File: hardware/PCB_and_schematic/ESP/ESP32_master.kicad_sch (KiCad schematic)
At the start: 0 parts

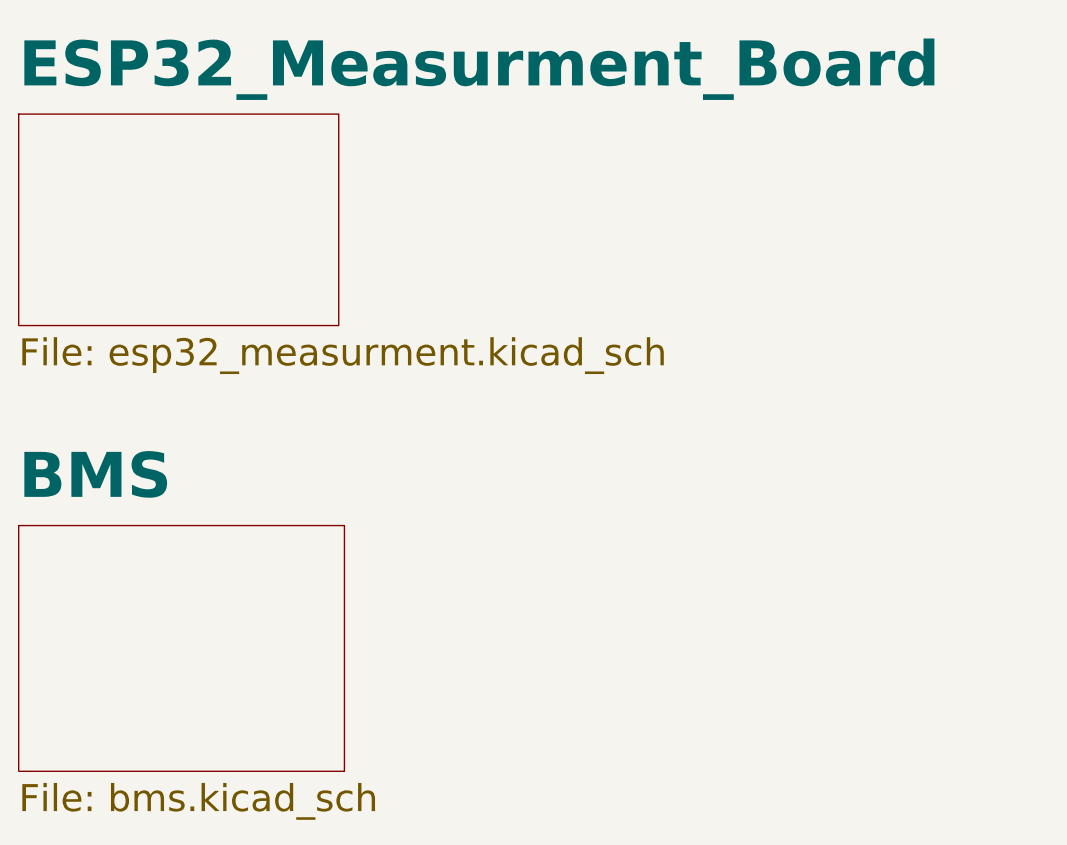
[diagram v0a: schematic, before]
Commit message: Add simulations and recheck schematics + cleanup
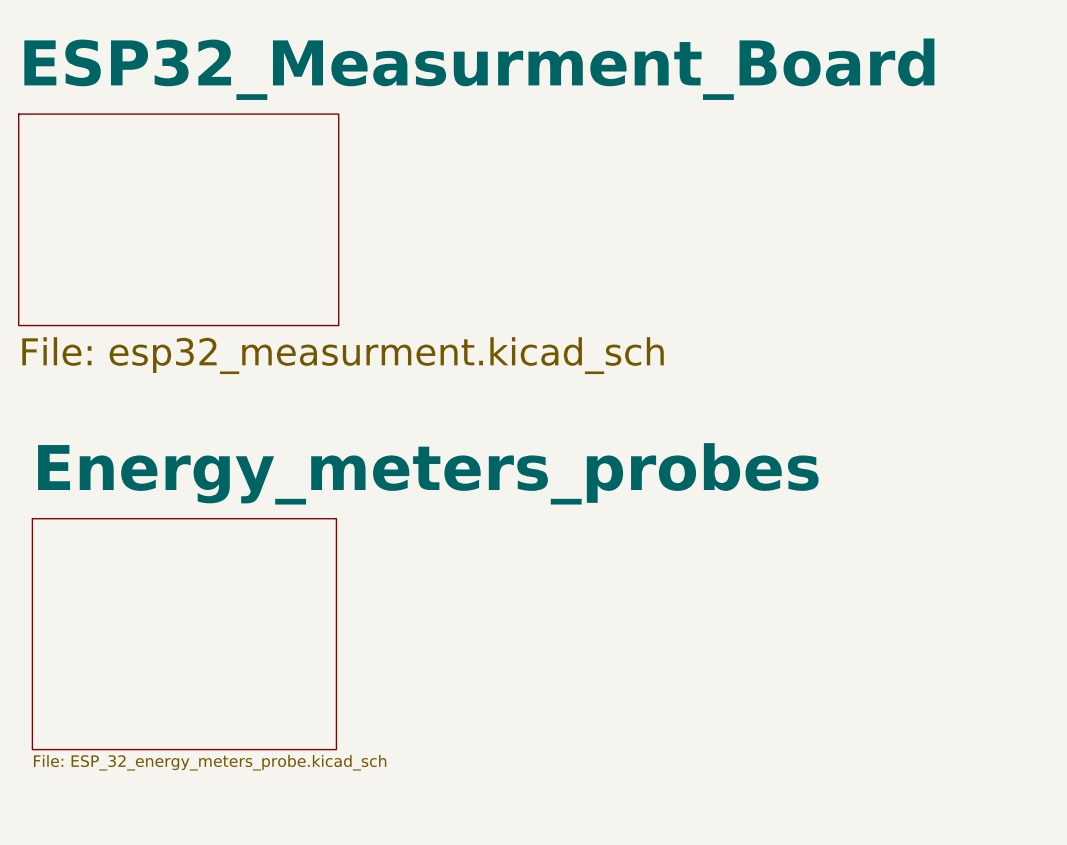
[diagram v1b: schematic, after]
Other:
- removed sheet BMS
- added sheet Energy_meters_probes (ESP_32_energy_meters_probe.kicad_sch)
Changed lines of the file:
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@@
 	(paper "A4" portrait)
 	(sheet
-		(at 24.13 80.01)
-		(size 36.195 27.305)
+		(at 25.654 79.248)
+		(size 33.782 25.654)
 		(fields_autoplaced yes)
 		(stroke
@@
 			(color 0 0 0 0.0000)
 		)
-		(property "Sheetname" "BMS"
-			(at 24.13 77.4334 0)
+		(property "Sheetname" "Energy_meters_probes"
+			(at 25.654 76.6714 0)
 			(effects
 				(font
@@
 			)
 		)
-		(property "Sheetfile" "bms.kicad_sch"
-			(at 24.13 108.5916 0)
+		(property "Sheetfile" "ESP_32_energy_meters_probe.kicad_sch"
+			(at 25.654 105.4866 0)
 			(effects
 				(font
-					(size 3 3)
+					(size 1.27 1.27)
 				)
 				(justify left top)
@@
 		)
 		(instances
-			(project "Balancer+ESP"
+			(project "ESP32_master"
 				(path "/555ba40f-9abb-4b99-82c6-07e888fda9fd"
 					(page "3")
@@
 		)
 		(instances
-			(project "Balancer+ESP"
+			(project "ESP32_master"
 				(path "/555ba40f-9abb-4b99-82c6-07e888fda9fd"
 					(page "2")

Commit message: Balancer routing
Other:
- removed sheet Energy_meters_probes
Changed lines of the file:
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@@
 	(paper "A4" portrait)
-	(sheet
-		(at 25.654 79.248)
-		(size 33.782 25.654)
-		(fields_autoplaced yes)
-		(stroke
-			(width 0.1524)
-			(type solid)
-		)
-		(fill
-			(color 0 0 0 0.0000)
-		)
-		(property "Sheetname" "Energy_meters_probes"
-			(at 25.654 76.6714 0)
-			(effects
-				(font
-					(size 5 5)
-					(bold yes)
-				)
-				(justify left bottom)
-			)
-		)
-		(property "Sheetfile" "ESP_32_energy_meters_probe.kicad_sch"
-			(at 25.654 105.4866 0)
-			(effects
-				(font
-					(size 1.27 1.27)
-				)
-				(justify left top)
-			)
-		)
-		(instances
-			(project "ESP32_master"
-				(path "/555ba40f-9abb-4b99-82c6-07e888fda9fd"
-					(page "3")
-				)
-			)
-		)
-	)
 	(sheet
 		(at 24.13 34.29)

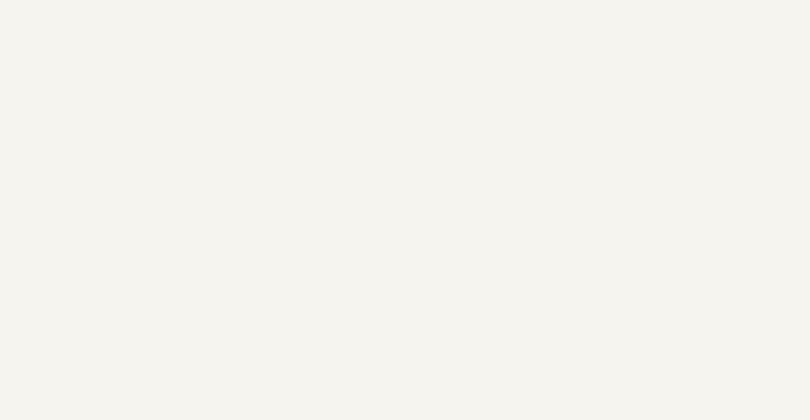
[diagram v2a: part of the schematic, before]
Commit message: Update of ESP32 PCB - parts positioning
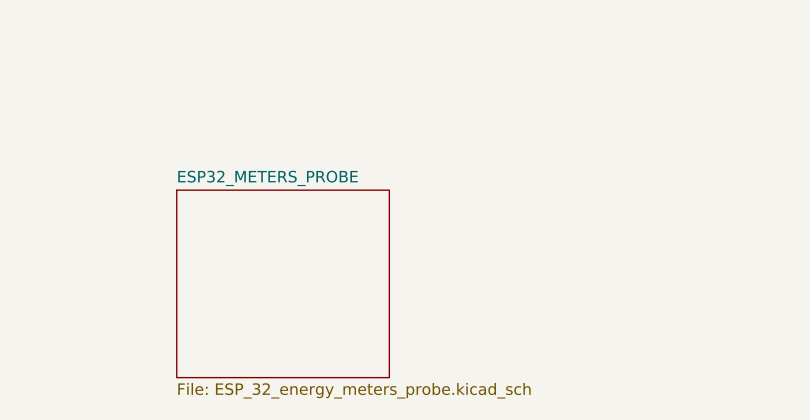
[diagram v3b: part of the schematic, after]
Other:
- added sheet ESP32_METERS_PROBE (ESP_32_energy_meters_probe.kicad_sch)
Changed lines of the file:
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@@
 	(paper "A4" portrait)
+	(sheet
+		(at 46.482 86.868)
+		(size 23.622 20.828)
+		(fields_autoplaced yes)
+		(stroke
+			(width 0.1524)
+			(type solid)
+		)
+		(fill
+			(color 0 0 0 0.0000)
+		)
+		(property "Sheetname" "ESP32_METERS_PROBE"
+			(at 46.482 86.1564 0)
+			(effects
+				(font
+					(size 1.27 1.27)
+				)
+				(justify left bottom)
+			)
+		)
+		(property "Sheetfile" "ESP_32_energy_meters_probe.kicad_sch"
+			(at 46.482 108.2806 0)
+			(effects
+				(font
+					(size 1.27 1.27)
+				)
+				(justify left top)
+			)
+		)
+		(instances
+			(project "ESP32_master"
+				(path "/555ba40f-9abb-4b99-82c6-07e888fda9fd"
+					(page "3")
+				)
+			)
+		)
+	)
 	(sheet
 		(at 24.13 34.29)
